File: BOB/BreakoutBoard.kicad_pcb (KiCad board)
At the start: 2 copper layers, 173 x 99 mm, 21 parts, among them J1 1706013, J10 Conn_01x04, J11 Conn_01x02, J12 Conn_01x02, J13 Conn_01x04, J14 Conn_01x04, J15 Conn_01x06, J2 Conn_01x18, J3 1706013, J4 Conn_01x06, J5 Conn_01x18, J6 Conn_01x18, J7 Conn_01x18, J8 1706013, J9 Conn_01x04

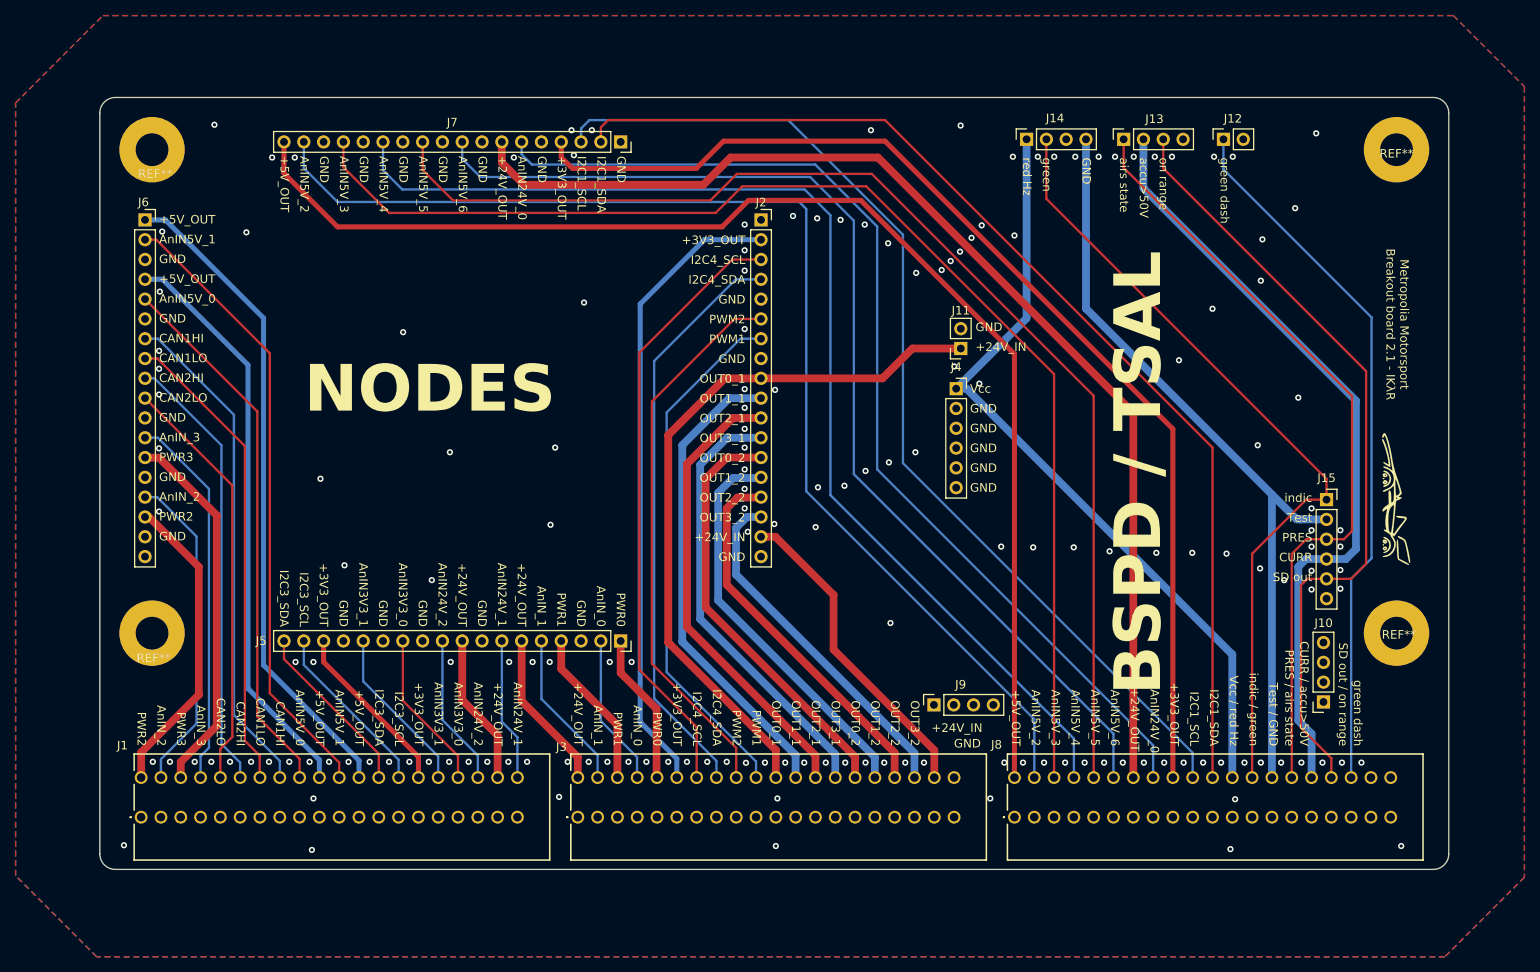
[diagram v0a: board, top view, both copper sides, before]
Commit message: BOB v2.1.2
- Reduced font size
- Fixed mistake with CAN numbers
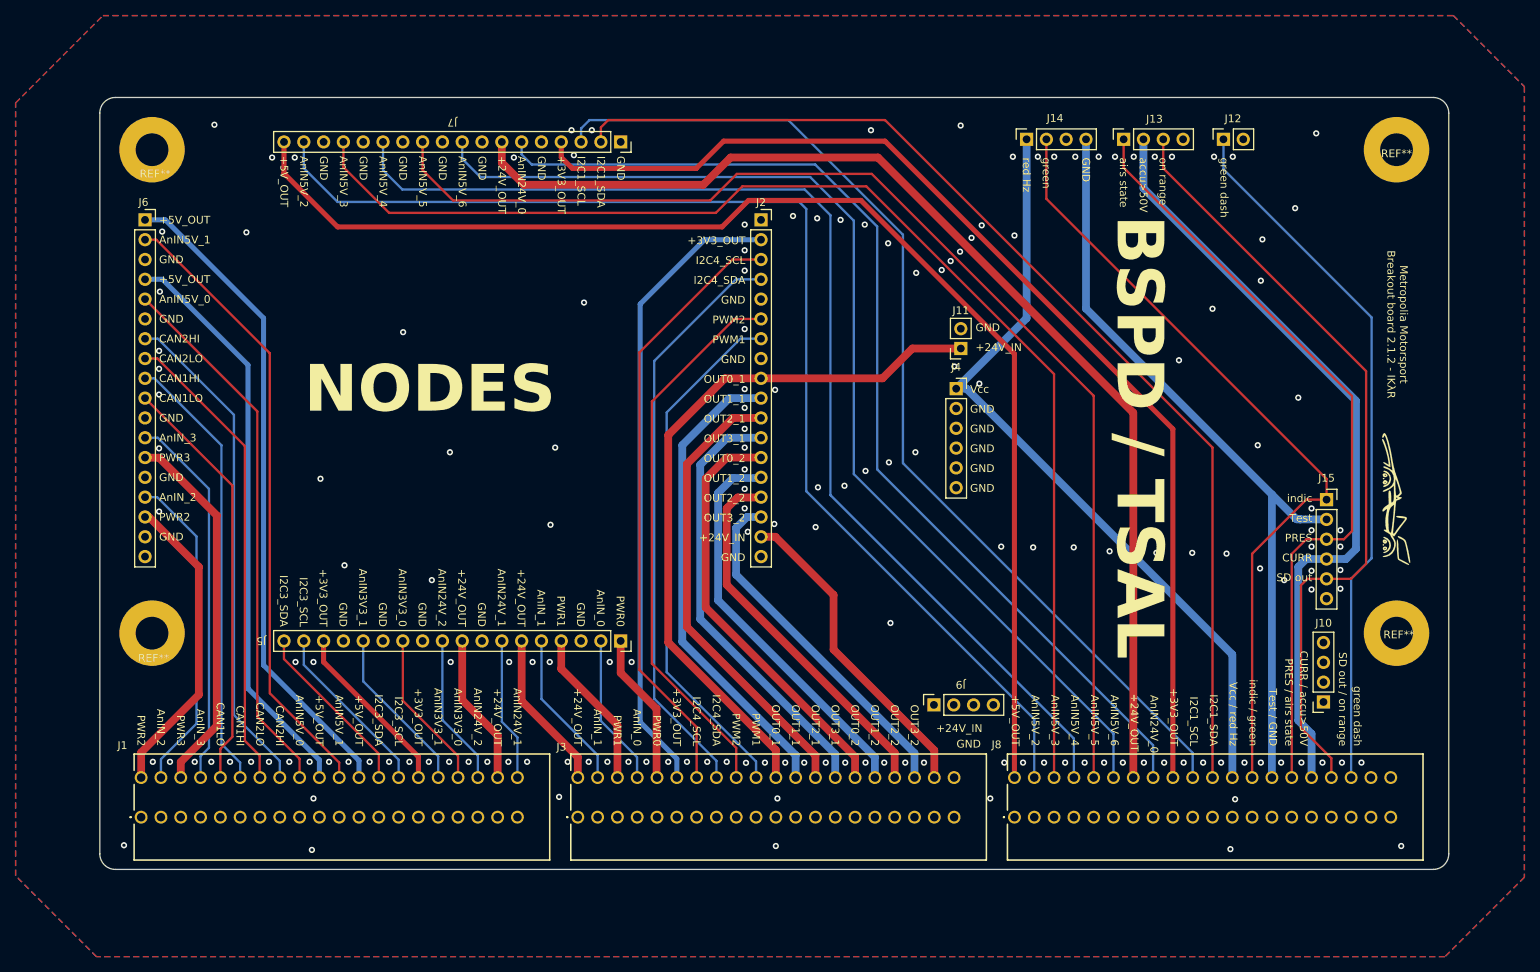
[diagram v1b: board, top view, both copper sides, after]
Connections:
- J1 pad 10: /CAN2LO -> /CAN1LO
- J1 pad 12: /CAN2HI -> /CAN1HI
- J1 pad 14: /CAN1LO -> /CAN2LO
- J1 pad 16: /CAN1HI -> /CAN2HI
- J6 pad 10: /CAN2LO -> /CAN1LO
- J6 pad 7: /CAN1HI -> /CAN2HI
- J6 pad 8: /CAN1LO -> /CAN2LO
- J6 pad 9: /CAN2HI -> /CAN1HI
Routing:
- net /CAN2HI: track 57.0 -> 64.4 mm
- net /CAN1HI: track 64.4 -> 57.0 mm
- net /CAN2LO: track 53.9 -> 60.8 mm
- net /CAN1LO: track 60.8 -> 53.9 mm
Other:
- board text added: "Metropolia Motorsport Breakout board 2.1.2 - IKλR"
- board text removed: "Metropolia Motorsport Breakout board 2.1 - IKλR"

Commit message: BOB v2.2
- New connector for OUT signals and input power pins (Connection for filter modules is not available on this version due to the size of connectors and maximum length of the board)
- Added two big holes for better and more stable connection in the car
- New layout and support for Nodes v2.2
- Created a combined design of 2.54mm connector for more efficient area usage
- PDF schematic added
- Other small visual changes

TODO:
- Change TSAL connection design, because of this issue the labels are not aligned
- Try to use double row connectors instead of just one row for more efficient space usage
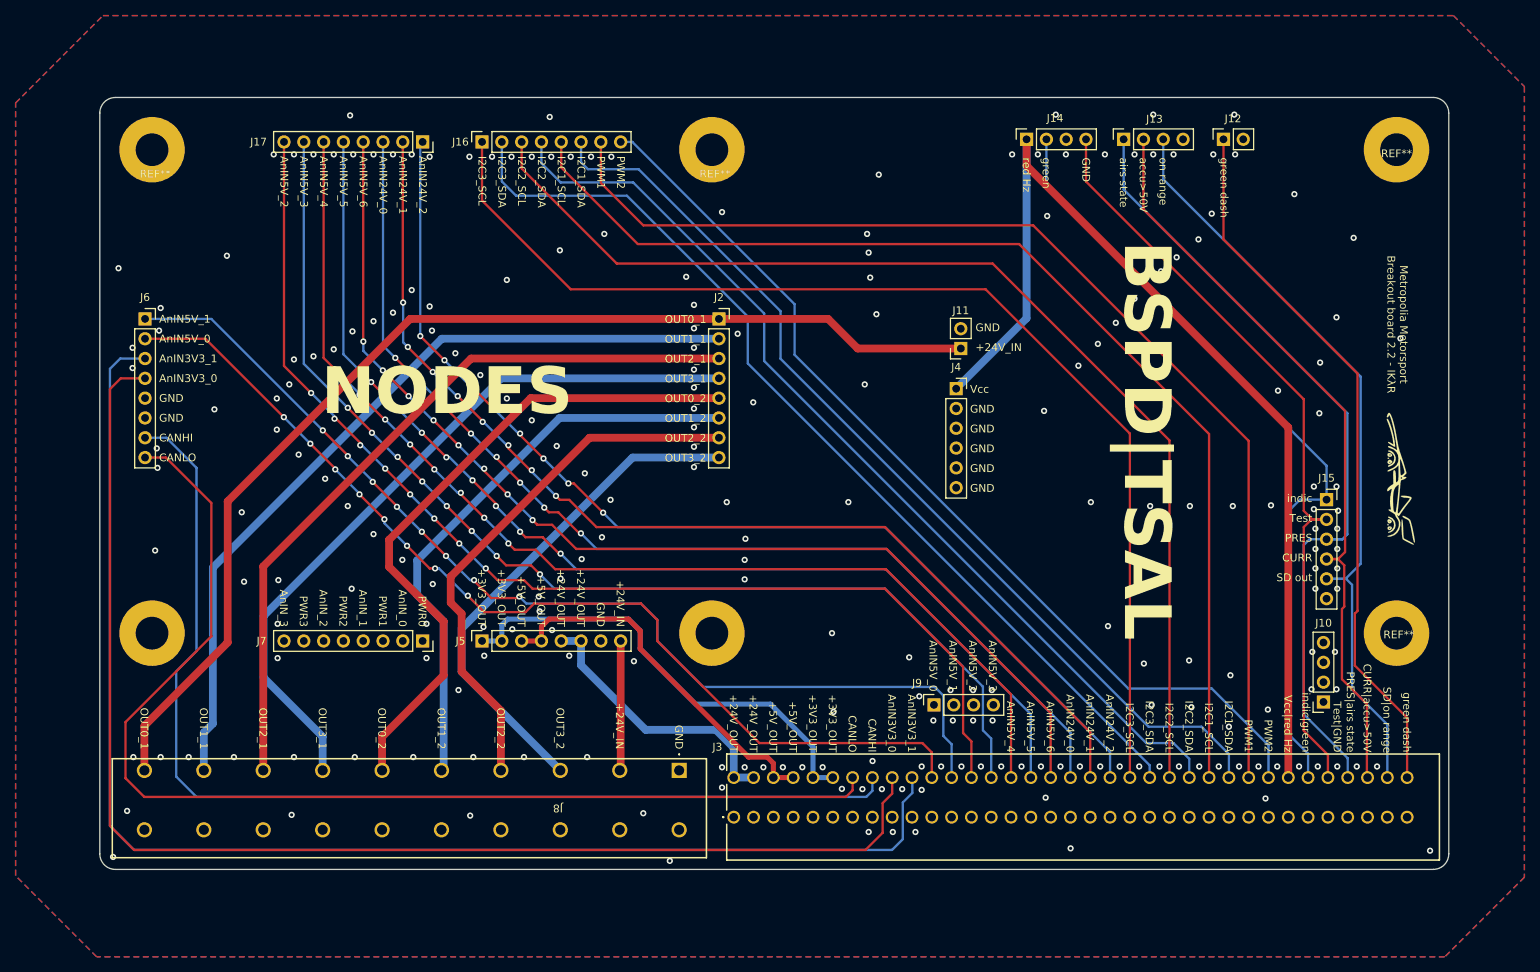
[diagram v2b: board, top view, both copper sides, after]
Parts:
- removed J1: 1706013, Connector_Phoenix_SPT:1706013
- added ?: , , F.Cu at (71.4, 113.4)
- added ?: , , F.Cu at (143.2, 113.4)
- added J16: Conn_01x08, Connector_PinSocket_2.54mm:PinSocket_1x08_P2.54mm_Vertical, F.Cu at (113.7, 50.4)
- added J17: Conn_01x08, Connector_PinSocket_2.54mm:PinSocket_1x08_P2.54mm_Vertical, F.Cu at (106.1, 50.4)
- J2, J5, J6, J7: value Conn_01x18 -> Conn_01x08; footprint Connector_PinSocket_2.54mm:PinSocket_1x18_P2.54mm_Vertical -> Connector_PinSocket_2.54mm:PinSocket_1x08_P2.54mm_Vertical
- J3: footprint Connector_Phoenix_SPT:1706013 -> Connector_Phoenix_SPT:35_con_Phoenix
- J8: value 1706013 -> ~; footprint Connector_Phoenix_SPT:1706013 -> Connector:1700884
- moved REF** 98.7 mm to (143.2, 51.4)
- moved J7 68.9 mm to (106.1, 114.4)
- moved J8 43.4 mm to (139.0, 131.0), turned to 180 degrees
- moved G*** 25.7 mm to (231.6, 93.6), turned to -90 degrees
- moved J3 20.0 mm to (146.0, 137.0)
- moved J5 17.8 mm to (113.7, 114.4), turned to 90 degrees
- moved J2 13.8 mm to (144.1, 73.1)
- moved J6 12.7 mm to (70.5, 73.1)
- moved G*** 2.67 mm to (231.6, 93.6)
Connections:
- J2 pad 1: unconnected-(J2-Pin_1-Pad1) -> /OUT0_1
- J2 pad 2: /+3V3_OUT2 -> /OUT1_1
- J2 pad 3: /I2C4_SCL -> /OUT2_1
- J2 pad 4: /I2C4_SDA -> /OUT3_1
- J2 pad 5: /GND -> /OUT0_2
- J2 pad 6: /PWM2 -> /OUT1_2
- J2 pad 7: /PWM1 -> /OUT2_2
- J2 pad 8: /GND -> /OUT3_2
- J3 pad 10: /PWR0 -> /+3V3_OUT
- J3 pad 12: /+3V3_OUT2 -> /+3V3_OUT
- J3 pad 14: /I2C4_SCL -> /CANLO
- J3 pad 16: /I2C4_SDA -> /CANHI
- J3 pad 18: /PWM2 -> /AnIN3V3_0
- J3 pad 2: /+24V_OUT1 -> /+24V_OUT
- J3 pad 20: /PWM1 -> /AnIN3V3_1
- J3 pad 21: /OUT0_1 -> unconnected-(J3-Pad21)
- J3 pad 22: unconnected-(J3-Pad22) -> /AnIN5V_0
- J3 pad 23: /OUT1_1 -> unconnected-(J3-Pad23)
- J3 pad 24: unconnected-(J3-Pad24) -> /AnIN5V_1
- J3 pad 25: /OUT2_1 -> unconnected-(J3-Pad25)
- J3 pad 26: unconnected-(J3-Pad26) -> /AnIN5V_2
- J3 pad 27: /OUT3_1 -> unconnected-(J3-Pad27)
- J3 pad 28: unconnected-(J3-Pad28) -> /AnIN5V_3
- J3 pad 29: /OUT0_2 -> unconnected-(J3-Pad29)
- J3 pad 30: unconnected-(J3-Pad30) -> /AnIN5V_4
- J3 pad 31: /OUT1_2 -> unconnected-(J3-Pad31)
- J3 pad 32: unconnected-(J3-Pad32) -> /AnIN5V_5
- J3 pad 33: /OUT2_2 -> unconnected-(J3-Pad33)
- J3 pad 34: unconnected-(J3-Pad34) -> /AnIN5V_6
- J3 pad 35: /OUT3_2 -> unconnected-(J3-Pad35)
- J3 pad 36: unconnected-(J3-Pad36) -> /AnIN24V_0
- J3 pad 37: /Vin -> unconnected-(J3-Pad37)
- J3 pad 38: unconnected-(J3-Pad38) -> /AnIN24V_1
- J3 pad 39: /GND -> unconnected-(J3-Pad39)
- J3 pad 4: /AnIN_1 -> /+24V_OUT
- J3 pad 40: unconnected-(J3-Pad40) -> /AnIN24V_2
- J3 pad 6: /PWR1 -> /+5V_OUT
- J3 pad 8: /AnIN_0 -> /+5V_OUT
- J5 pad 1: /PWR0 -> /+3V3_OUT
- J5 pad 2: /AnIN_0 -> /+3V3_OUT
- J5 pad 3: /GND -> /+5V_OUT
- J5 pad 4: /PWR1 -> /+5V_OUT
- J5 pad 5: /AnIN_1 -> /+24V_OUT
- J5 pad 6: /+24V_OUT1 -> /+24V_OUT
- J5 pad 7: /AnIN24V_1 -> /GND
- J5 pad 8: /GND -> /Vin
- J6 pad 1: /+5V_OUT1 -> /AnIN5V_1
- J6 pad 2: /AnIN5V_1 -> /AnIN5V_0
- J6 pad 3: /GND -> /AnIN3V3_1
- J6 pad 4: /+5V_OUT0 -> /AnIN3V3_0
- J6 pad 5: /AnIN5V_0 -> /GND
- J6 pad 7: /CAN2HI -> /CANHI
- J6 pad 8: /CAN2LO -> /CANLO
- J7 pad 1: /GND -> /PWR0
- J7 pad 2: /I2C1_SDA -> /AnIN_0
- J7 pad 3: /I2C1_SCL -> /PWR1
- J7 pad 4: /+3V3_OUT0 -> /AnIN_1
- J7 pad 5: /GND -> /PWR2
- J7 pad 6: /AnIN24V_0 -> /AnIN_2
- J7 pad 7: /+24V_OUT0 -> /PWR3
- J7 pad 8: /GND -> /AnIN_3
- J8 pad 1: unconnected-(J8-Pad1) -> /GND
- J8 pad 10: /AnIN5V_5 -> /OUT0_1
- J8 pad 12: /AnIN5V_6 -> unconnected-(J8-Pad12)
- J8 pad 14: /+24V_OUT0 -> unconnected-(J8-Pad14)
- J8 pad 16: /AnIN24V_0 -> unconnected-(J8-Pad16)
- J8 pad 18: /+3V3_OUT0 -> unconnected-(J8-Pad18)
- J8 pad 2: /+5V_OUT2 -> /Vin
- J8 pad 20: /I2C1_SCL -> unconnected-(J8-Pad20)
- J8 pad 3: unconnected-(J8-Pad3) -> /OUT3_2
- J8 pad 4: /AnIN5V_2 -> /OUT2_2
- J8 pad 5: unconnected-(J8-Pad5) -> /OUT1_2
- J8 pad 6: /AnIN5V_3 -> /OUT0_2
- J8 pad 7: unconnected-(J8-Pad7) -> /OUT3_1
- J8 pad 8: /AnIN5V_4 -> /OUT2_1
- J8 pad 9: unconnected-(J8-Pad9) -> /OUT1_1
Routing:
- net /+5V_OUT2: track 164.4 -> 0.00 mm
- net /AnIN3V3_1: track 21.5 -> 175.6 mm
- net /AnIN3V3_0: track 20.5 -> 170.0 mm
- net /CANLO: track 0.00 -> 147.0 mm
- net /+24V_OUT0: track 146.6 -> 0.00 mm
- net /I2C2_SCL: track 0.00 -> 144.2 mm
- net /+3V3_OUT0: track 142.5 -> 0.00 mm
- net /CANHI: track 0.00 -> 141.3 mm
- net /I2C3_SCL: track 22.6 -> 147.1 mm
- net /I2C2_SDA: track 0.00 -> 123.4 mm
- net /AnIN24V_1: track 18.3 -> 140.8 mm, vias 0 -> 8
- net /AnIN24V_2: track 19.4 -> 139.0 mm, vias 0 -> 8
- net /I2C3_SDA: track 22.6 -> 124.3 mm
- net /+5V_OUT1: track 84.4 -> 0.00 mm
- net /+3V3_OUT2: track 81.6 -> 0.00 mm
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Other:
- board text added: "BSPD|TSAL"
- board text added: "CANHI"
- board text added: "CANLO"
- board text added: "CURR|accu>50V"
- board text added: "I2C2_SCL"
- board text added: "I2C2_SDA"
- board text added: "Metropolia Motorsport Breakout board 2.2 - IKλR"
- board text added: "PRES|airs state"
- board text added: "SD|on range"
- board text added: "Test|GND"
- board text added: "Vcc|red Hz"
- board text added: "indic|green"
- board text removed: "BSPD / TSAL"
- board text removed: "CAN1HI"
- board text removed: "CAN1LO"
- board text removed: "CAN2HI"
- board text removed: "CAN2LO"
- board text removed: "CURR / accu>50V"
- board text removed: "I2C4_SCL"
- board text removed: "I2C4_SDA"
- board text removed: "Metropolia Motorsport Breakout board 2.1.2 - IKλR"
- board text removed: "PRES / airs state"
- board text removed: "SD out / on range"
- board text removed: "Test / GND"
- board text removed: "Vcc / red Hz"
- board text removed: "indic / green"

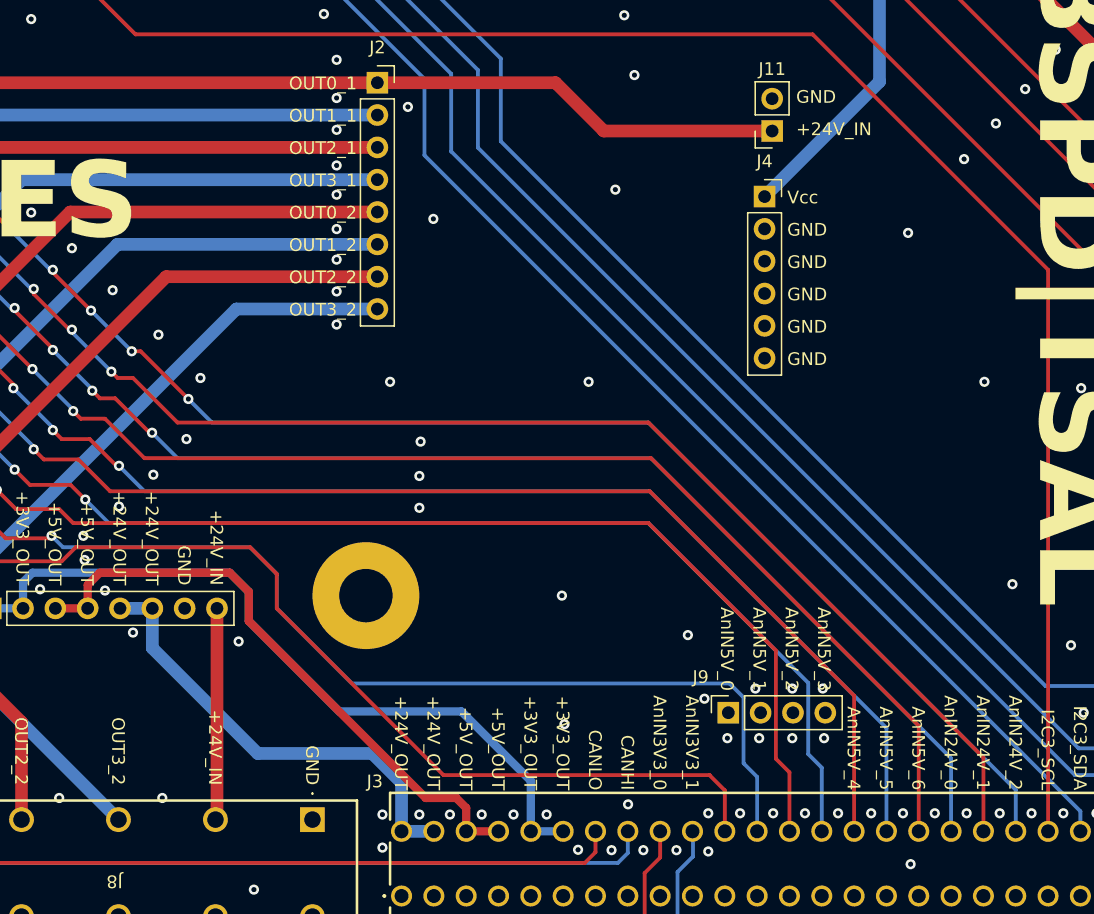
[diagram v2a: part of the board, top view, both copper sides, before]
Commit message: v2.2.1
-TSAL now connected to +24V_IN instead of OUT0_1
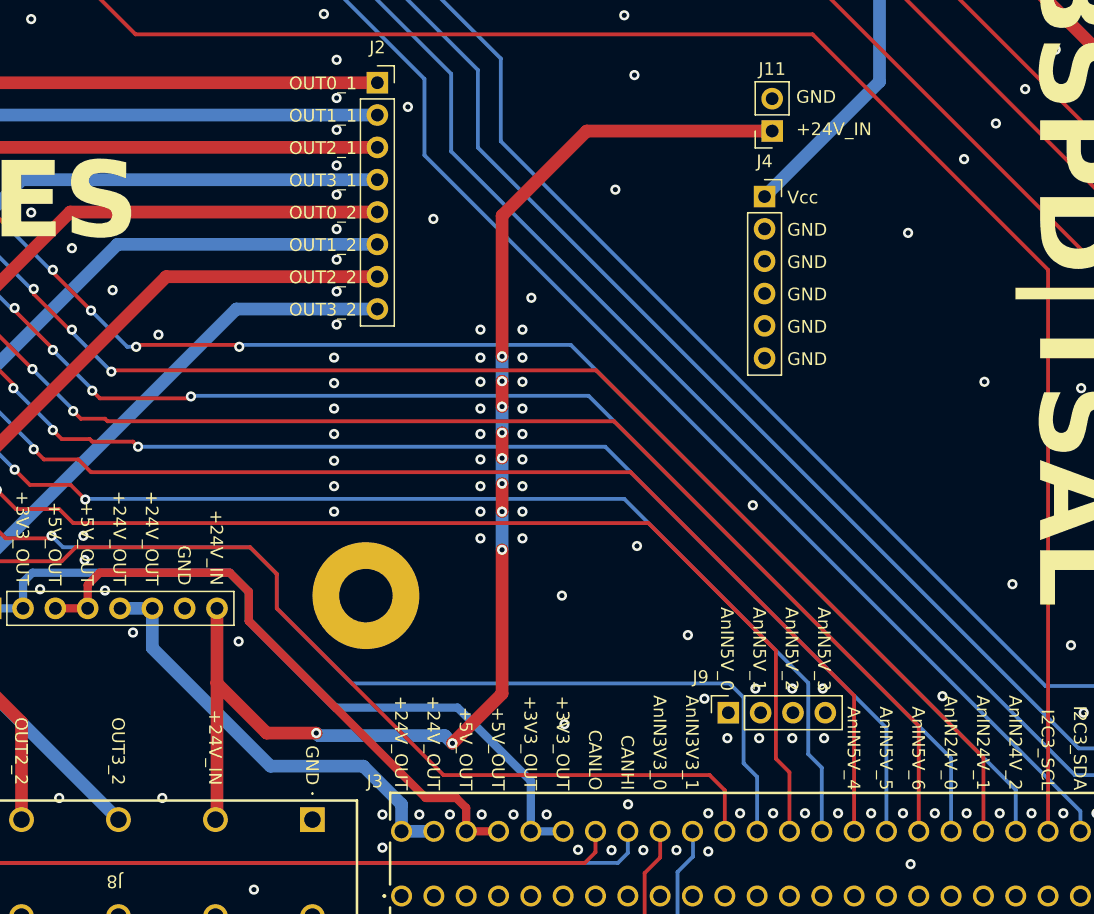
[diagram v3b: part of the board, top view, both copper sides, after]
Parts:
- removed the G*** at (231.6, 93.6)
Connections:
- J11 pad 1: /OUT0_1 -> /Vin
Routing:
- net /Vin: track 16.6 -> 104.2 mm, vias 0 -> 10
- net /OUT0_1: track 144.2 -> 111.8 mm
- net /+24V_OUT: track 36.0 -> 35.0 mm
- net /GND: vias 230 -> 250
